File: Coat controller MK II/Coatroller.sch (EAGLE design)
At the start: 9 parts, among them U1 ATMEGA328P_PDIP, U2 V_REG_LDOSMD, Y1 ABM3B-16.000MHZ-B2-T

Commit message: Fixed usb direction and fixed some routing
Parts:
- added BUTTON: 1751248, con-phoenix-350:1751248
- added PULLDOWN: 10K, SparkFun-Resistors:10KOHM-1/10W-1%(0603)0603
- added U$10, U$11, U$12, U$13, U$14, U$15, U$16, U$17, U$18, U$19, U$2, U$20, U$21, U$3, U$4, U$5, U$6, U$7, U$8, U$9: REMOTE-BUTTON, myparts:REMOTE-BUTTON
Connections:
- new net BUTTONPIN: BUTTON-2.K, PULLDOWN.2, U1.PD6(AIN0)
- net GROUND: now also PULLDOWN.1
- net VCC: now also BUTTON-1.K
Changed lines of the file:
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@@
 <part name="PIN" library="con-amp-micromatch" deviceset="MICROMATCH-4" device=""/>
 <part name="C2" library="SparkFun-Capacitors" deviceset="2.2UF50V10%(1206)" device=""/>
+<part name="U$2" library="myparts" deviceset="REMOTE-BUTTON" device=""/>
+<part name="U$3" library="myparts" deviceset="REMOTE-BUTTON" device=""/>
+<part name="U$4" library="myparts" deviceset="REMOTE-BUTTON" device=""/>
+<part name="U$5" library="myparts" deviceset="REMOTE-BUTTON" device=""/>
+<part name="U$6" library="myparts" deviceset="REMOTE-BUTTON" device=""/>
+<part name="U$7" library="myparts" deviceset="REMOTE-BUTTON" device=""/>
+<part name="U$8" library="myparts" deviceset="REMOTE-BUTTON" device=""/>
+<part name="U$9" library="myparts" deviceset="REMOTE-BUTTON" device=""/>
+<part name="U$10" library="myparts" deviceset="REMOTE-BUTTON" device=""/>
+<part name="U$11" library="myparts" deviceset="REMOTE-BUTTON" device=""/>
+<part name="U$12" library="myparts" deviceset="REMOTE-BUTTON" device=""/>
+<part name="U$13" library="myparts" deviceset="REMOTE-BUTTON" device=""/>
+<part name="U$14" library="myparts" deviceset="REMOTE-BUTTON" device=""/>
+<part name="U$15" library="myparts" deviceset="REMOTE-BUTTON" device=""/>
+<part name="U$16" library="myparts" deviceset="REMOTE-BUTTON" device=""/>
+<part name="U$17" library="myparts" deviceset="REMOTE-BUTTON" device=""/>
+<part name="U$18" library="myparts" deviceset="REMOTE-BUTTON" device=""/>
+<part name="U$19" library="myparts" deviceset="REMOTE-BUTTON" device=""/>
+<part name="U$20" library="myparts" deviceset="REMOTE-BUTTON" device=""/>
+<part name="U$21" library="myparts" deviceset="REMOTE-BUTTON" device=""/>
+<part name="BUTTON" library="con-phoenix-350" deviceset="1751248" device=""/>
+<part name="PULLDOWN" library="SparkFun-Resistors" deviceset="10KOHM-1/10W-1%(0603)" device="0603" value="10K"/>
 </parts>
 <sheets>
@@
 <instance part="PIN" gate="-4" x="157.48" y="25.4" rot="R180"/>
 <instance part="C2" gate="G$1" x="88.9" y="73.66" rot="R270"/>
+<instance part="BUTTON" gate="-1" x="-5.08" y="83.82" rot="R180"/>
+<instance part="BUTTON" gate="-2" x="-5.08" y="76.2" rot="R180"/>
+<instance part="PULLDOWN" gate="G$1" x="25.4" y="76.2" rot="R180"/>
 </instances>
 <busses>
@@
 <wire x1="63.5" y1="55.88" x2="63.5" y2="60.96" width="0.1524" layer="91"/>
 <pinref part="POWEROUT" gate="-2" pin="K"/>
-<wire x1="63.5" y1="60.96" x2="63.5" y2="78.74" width="0.1524" layer="91"/>
+<wire x1="63.5" y1="60.96" x2="63.5" y2="76.2" width="0.1524" layer="91"/>
+<wire x1="63.5" y1="76.2" x2="63.5" y2="78.74" width="0.1524" layer="91"/>
 <wire x1="63.5" y1="78.74" x2="63.5" y2="81.28" width="0.1524" layer="91"/>
 <wire x1="63.5" y1="81.28" x2="63.5" y2="83.82" width="0.1524" layer="91"/>
@@
 <wire x1="91.44" y1="81.28" x2="63.5" y2="81.28" width="0.1524" layer="91"/>
 <junction x="63.5" y="81.28"/>
+<pinref part="PULLDOWN" gate="G$1" pin="1"/>
+<wire x1="30.48" y1="76.2" x2="63.5" y2="76.2" width="0.1524" layer="91"/>
+<junction x="63.5" y="76.2"/>
 </segment>
 </net>
@@
 <pinref part="POWERINPUT" gate="-2" pin="K"/>
 <wire x1="58.42" y1="55.88" x2="58.42" y2="66.04" width="0.1524" layer="91"/>
-<wire x1="58.42" y1="66.04" x2="58.42" y2="96.52" width="0.1524" layer="91"/>
+<wire x1="58.42" y1="66.04" x2="58.42" y2="83.82" width="0.1524" layer="91"/>
+<wire x1="58.42" y1="83.82" x2="58.42" y2="96.52" width="0.1524" layer="91"/>
 <wire x1="58.42" y1="96.52" x2="58.42" y2="101.6" width="0.1524" layer="91"/>
 <wire x1="58.42" y1="101.6" x2="66.04" y2="101.6" width="0.1524" layer="91"/>
@@
 <junction x="58.42" y="55.88"/>
 <label x="114.3" y="35.56" size="1.778" layer="95"/>
+<pinref part="BUTTON" gate="-1" pin="K"/>
+<wire x1="-2.54" y1="83.82" x2="58.42" y2="83.82" width="0.1524" layer="91"/>
+<junction x="58.42" y="83.82"/>
 </segment>
 </net>
@@
 </segment>
 </net>
+<net name="BUTTONPIN" class="0">
+<segment>
+<pinref part="U1" gate="G$1" pin="PD6(AIN0)"/>
+<wire x1="167.64" y1="71.12" x2="198.12" y2="71.12" width="0.1524" layer="91"/>
+<wire x1="198.12" y1="71.12" x2="198.12" y2="5.08" width="0.1524" layer="91"/>
+<wire x1="198.12" y1="5.08" x2="5.08" y2="5.08" width="0.1524" layer="91"/>
+<pinref part="BUTTON" gate="-2" pin="K"/>
+<pinref part="PULLDOWN" gate="G$1" pin="2"/>
+<wire x1="-2.54" y1="76.2" x2="5.08" y2="76.2" width="0.1524" layer="91"/>
+<wire x1="5.08" y1="76.2" x2="20.32" y2="76.2" width="0.1524" layer="91"/>
+<wire x1="5.08" y1="5.08" x2="5.08" y2="76.2" width="0.1524" layer="91"/>
+<junction x="5.08" y="76.2"/>
+</segment>
+</net>

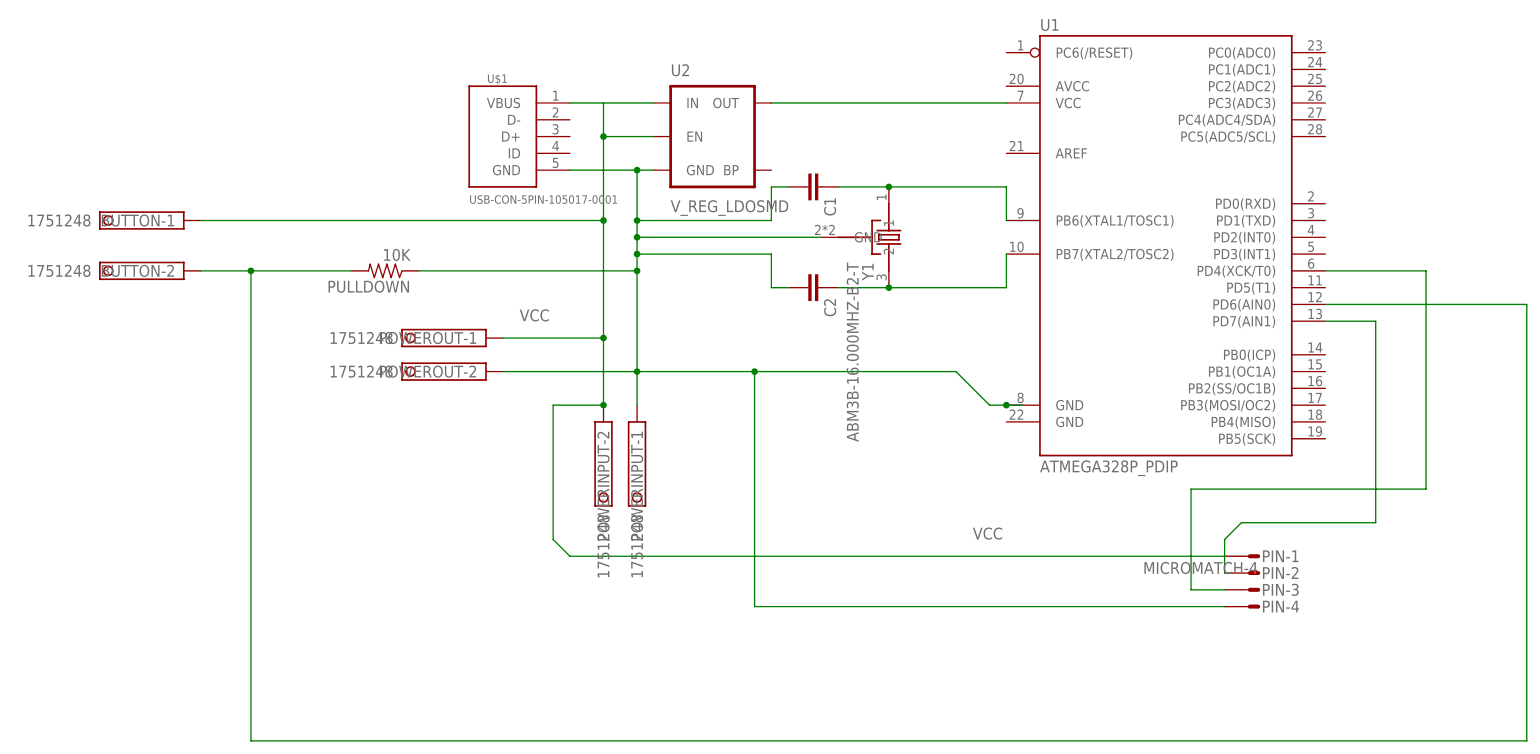
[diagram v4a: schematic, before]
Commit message: rotated micromatch to proper direction and rerouted. Fixed a few crossed routes
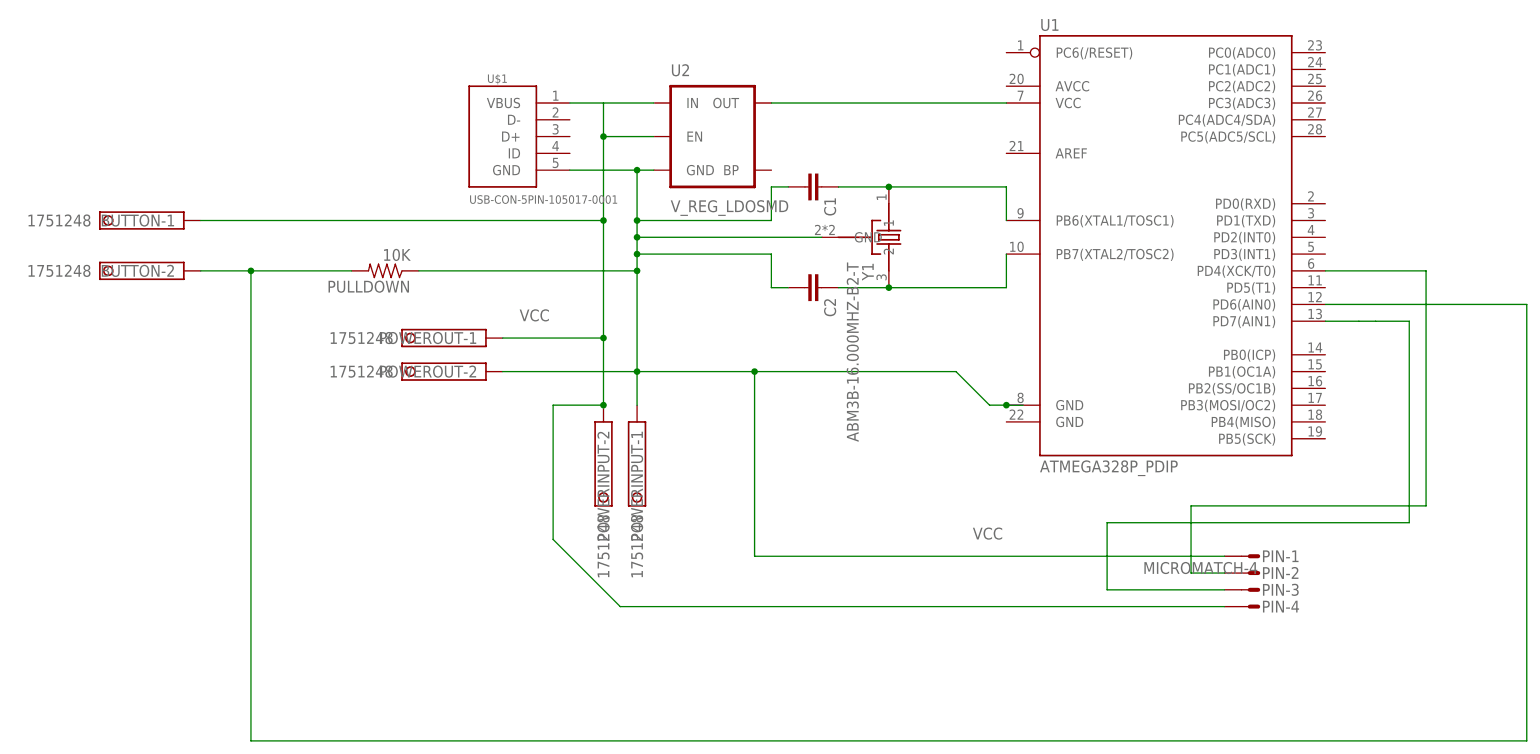
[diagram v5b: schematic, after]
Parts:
- removed U$10, U$11, U$12, U$13, U$14, U$15, U$16, U$17, U$18, U$19, U$2, U$20, U$21, U$3, U$4, U$5, U$6, U$7, U$8, U$9: REMOTE-BUTTON, myparts:REMOTE-BUTTON
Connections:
- net CLOCK: now also PIN-2.S; no longer PIN-3.S
- net DATA: now also PIN-3.S; no longer PIN-2.S
- net GROUND: now also PIN-1.S; no longer PIN-4.S
- net VCC: now also PIN-4.S; no longer PIN-1.S

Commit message: expect this is production level
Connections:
- net GROUND: now also U1.GND@2
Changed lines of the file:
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@@
 <junction x="81.28" y="60.96"/>
 <pinref part="C1" gate="G$1" pin="2"/>
-<wire x1="81.28" y1="33.02" x2="81.28" y2="60.96" width="0.1524" layer="91"/>
+<wire x1="81.28" y1="33.02" x2="81.28" y2="53.34" width="0.1524" layer="91"/>
+<wire x1="81.28" y1="53.34" x2="81.28" y2="60.96" width="0.1524" layer="91"/>
 <wire x1="86.36" y1="88.9" x2="83.82" y2="88.9" width="0.1524" layer="91"/>
 <wire x1="83.82" y1="88.9" x2="83.82" y2="83.82" width="0.1524" layer="91"/>
@@
 <pinref part="PIN" gate="-1" pin="S"/>
 <wire x1="152.4" y1="33.02" x2="81.28" y2="33.02" width="0.1524" layer="91"/>
+<pinref part="U1" gate="G$1" pin="GND@2"/>
+<wire x1="119.38" y1="53.34" x2="81.28" y2="53.34" width="0.1524" layer="91"/>
+<junction x="81.28" y="53.34"/>
 </segment>
 </net>
